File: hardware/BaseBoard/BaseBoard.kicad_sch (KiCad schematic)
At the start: 91 parts, among them J1 I2C, J1-ESP1 ESP-1-L, J1-ESP2 ESP-1-L, J1-ESP3 ESP-1-L, J1-ESP4 ESP-1-L, J1-ESP5 ESP-1-L, J1-ESP6 ESP-1-L, J1-ESP7 ESP-1-L, J1-ESP8 ESP-1-L, J2 3V3P0_7, J2-ESP1 ESP-1-R, J2-ESP2 ESP-1-R, J2-ESP3 ESP-1-R, J2-ESP4 ESP-1-R, J2-ESP5 ESP-1-R, J2-ESP6 ESP-1-R, J2-ESP7 ESP-1-R, J2-ESP8 ESP-1-R, J3-BUS1 BUS1-IN1, J3-BUS2 BUS1-IN1, J3-BUS3 BUS1-IN1, J3-BUS4 BUS1-IN1, J3-BUS5 BUS1-IN1, J3-BUS6 BUS1-IN1, J3-BUS7 BUS1-IN1, J3-BUS8 BUS1-IN1, J4-BUS1 BUS1-IN2, J4-BUS2 BUS1-IN2, J4-BUS3 BUS1-IN2, J4-BUS4 BUS1-IN2, J4-BUS5 BUS1-IN2, J4-BUS6 BUS1-IN2, J4-BUS7 BUS1-IN2, J4-BUS8 BUS1-IN2, J5-BUS1 BUS1-OUT, J5-BUS2 BUS1-OUT, J5-BUS3 BUS1-OUT, J5-BUS4 BUS1-OUT, J5-BUS5 BUS1-OUT, J5-BUS6 BUS1-OUT, J5-BUS7 BUS1-OUT, J5-BUS8 BUS1-OUT, Q1-ESP1 2N3904, Q1-ESP2 2N3904, Q1-ESP3 2N3904, Q1-ESP4 2N3904, Q1-ESP5 2N3904, Q1-ESP6 2N3904, Q1-ESP7 2N3904, Q1-ESP8 2N3904, Q2-ESP1 AO3401A, Q2-ESP2 AO3401A, Q2-ESP3 AO3401A, Q2-ESP4 AO3401A, Q2-ESP5 AO3401A, Q2-ESP6 AO3401A, Q2-ESP7 AO3401A, Q2-ESP8 AO3401A, U1 AMS1117-3.3

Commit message: Small optimizations.
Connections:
- net +5V: now also SW-ESP1.6, SW-ESP2.6, SW-ESP3.6, SW-ESP4.6, SW-ESP5.6, SW-ESP6.6, SW-ESP7.6, SW-ESP8.6
- net SWPIN-ESP5: now also J2.8 (Pin_8); no longer J2.5 (Pin_5)
- net SWPIN-ESP6: now also J2.7 (Pin_7); no longer J2.6 (Pin_6)
- net SWPIN-ESP7: now also J2.6 (Pin_6); no longer J2.7 (Pin_7)
- net SWPIN-ESP8: now also J2.5 (Pin_5); no longer J2.8 (Pin_8)
- no-connect marks 97 -> 89

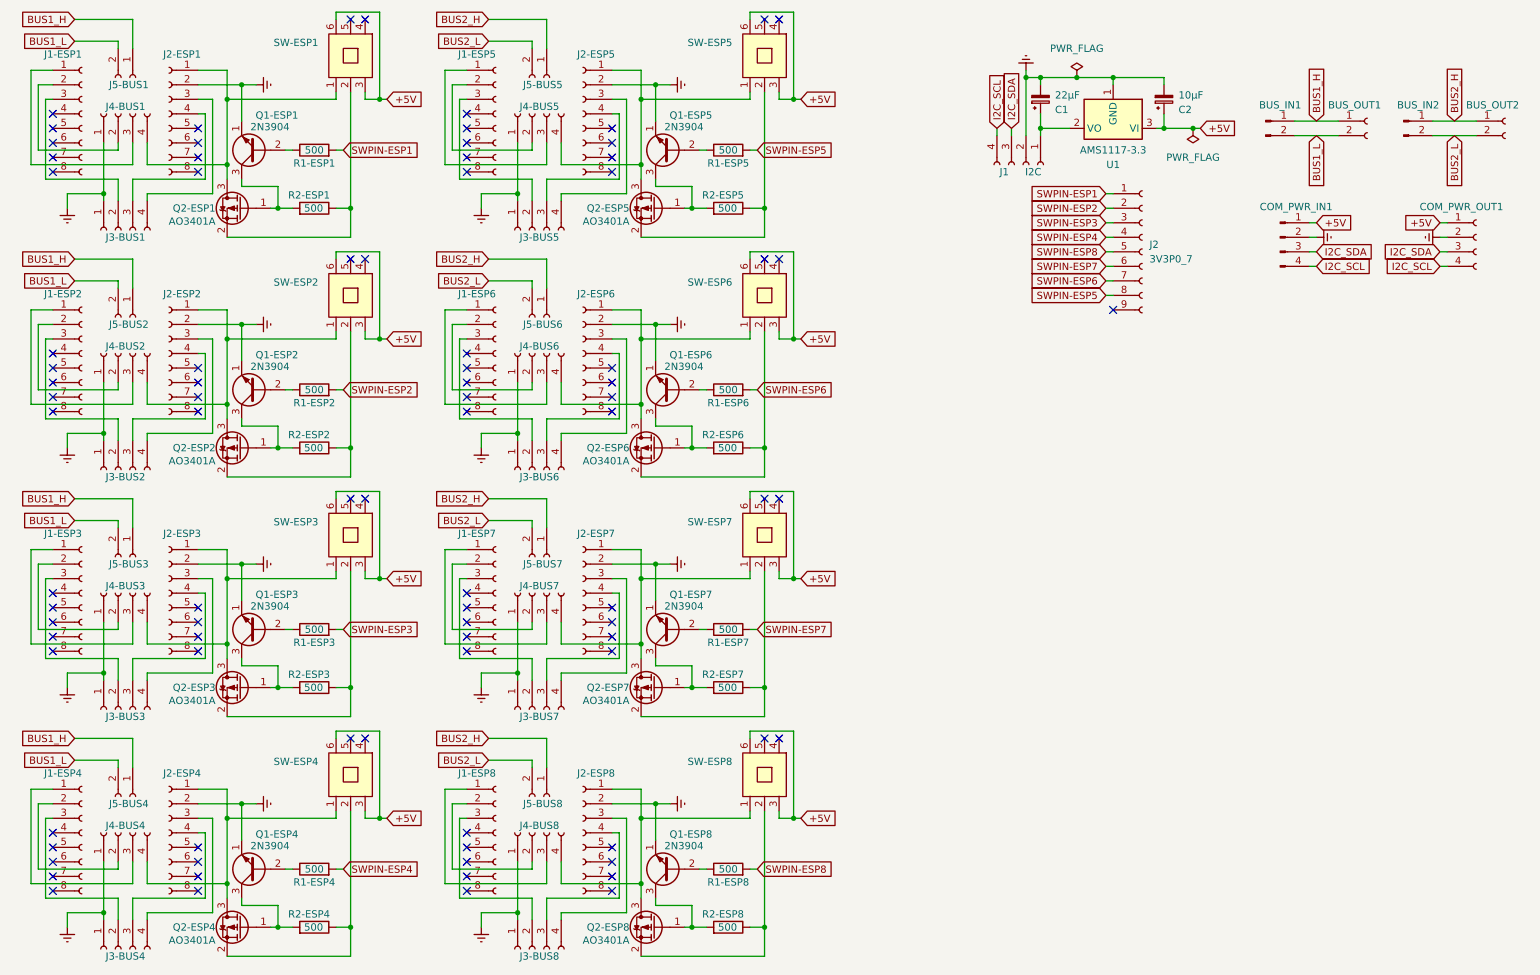
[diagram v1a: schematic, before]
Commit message: Added some more labels.
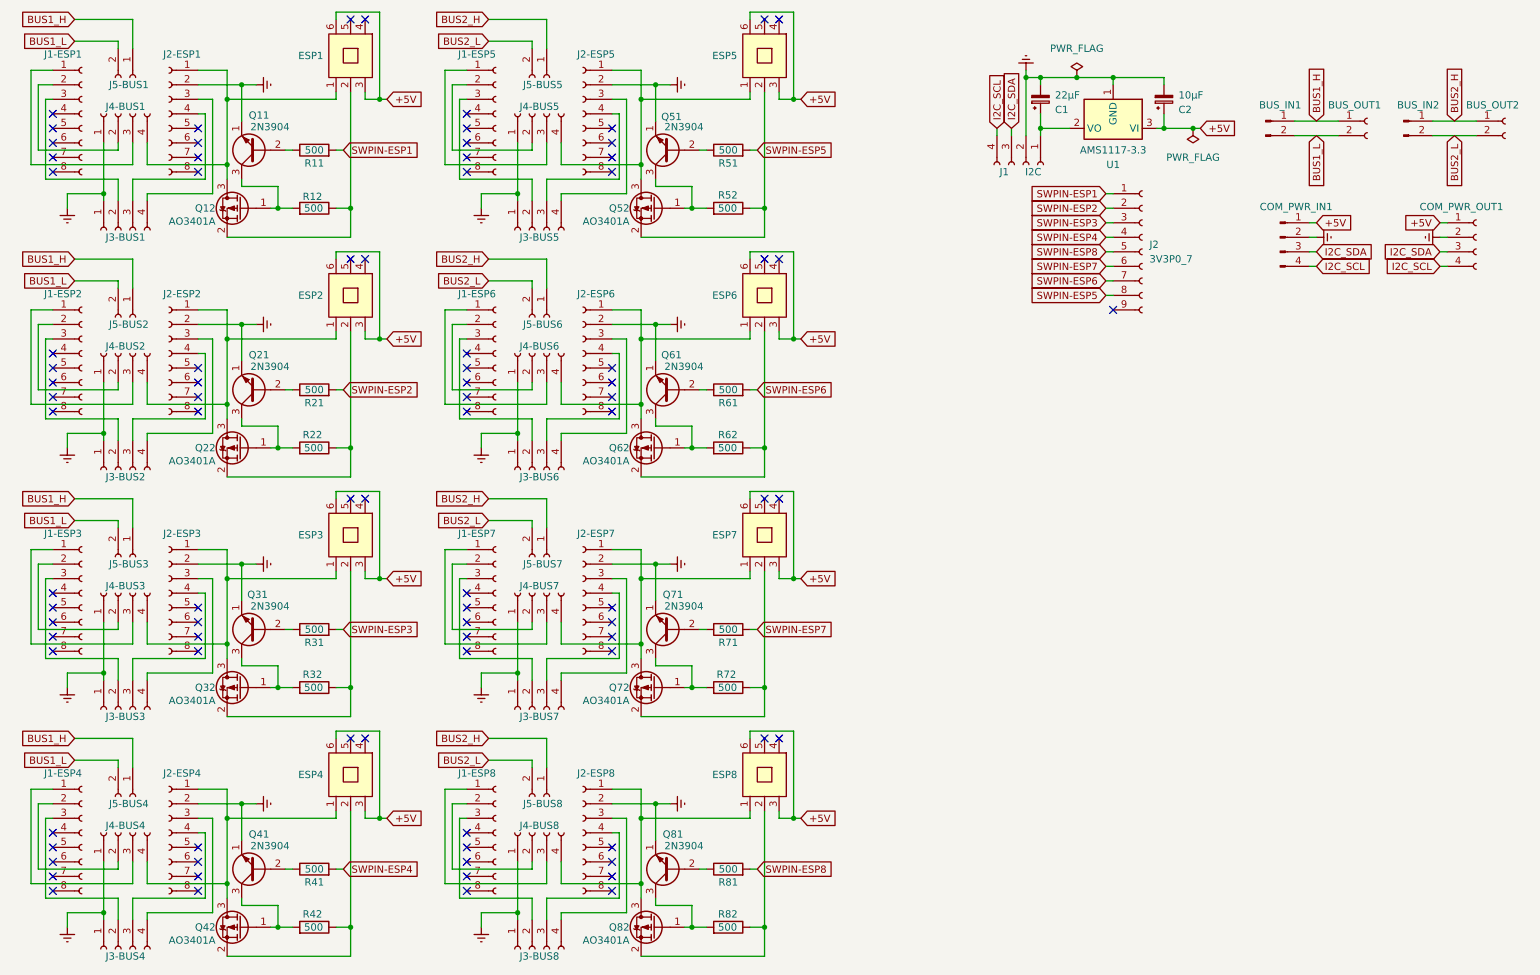
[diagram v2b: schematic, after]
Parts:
- renumbered SW-ESP1 to ESP1, SW-ESP2 to ESP2, SW-ESP3 to ESP3, SW-ESP4 to ESP4, SW-ESP5 to ESP5, SW-ESP6 to ESP6, SW-ESP7 to ESP7, SW-ESP8 to ESP8, Q1-ESP1 to Q11, Q2-ESP1 to Q12, Q1-ESP2 to Q21, Q2-ESP2 to Q22, Q1-ESP3 to Q31, Q2-ESP3 to Q32, Q1-ESP4 to Q41, Q2-ESP4 to Q42, Q1-ESP5 to Q51, Q2-ESP5 to Q52, Q1-ESP6 to Q61, Q2-ESP6 to Q62, Q1-ESP7 to Q71, Q2-ESP7 to Q72, Q1-ESP8 to Q81, Q2-ESP8 to Q82, R1-ESP1 to R11, R2-ESP1 to R12, R1-ESP2 to R21, R2-ESP2 to R22, R1-ESP3 to R31, R2-ESP3 to R32, R1-ESP4 to R41, R2-ESP4 to R42, R1-ESP5 to R51, R2-ESP5 to R52, R1-ESP6 to R61, R2-ESP6 to R62, R1-ESP7 to R71, R2-ESP7 to R72, R1-ESP8 to R81, R2-ESP8 to R82

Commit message: Replaced two one row headers with one two row header.
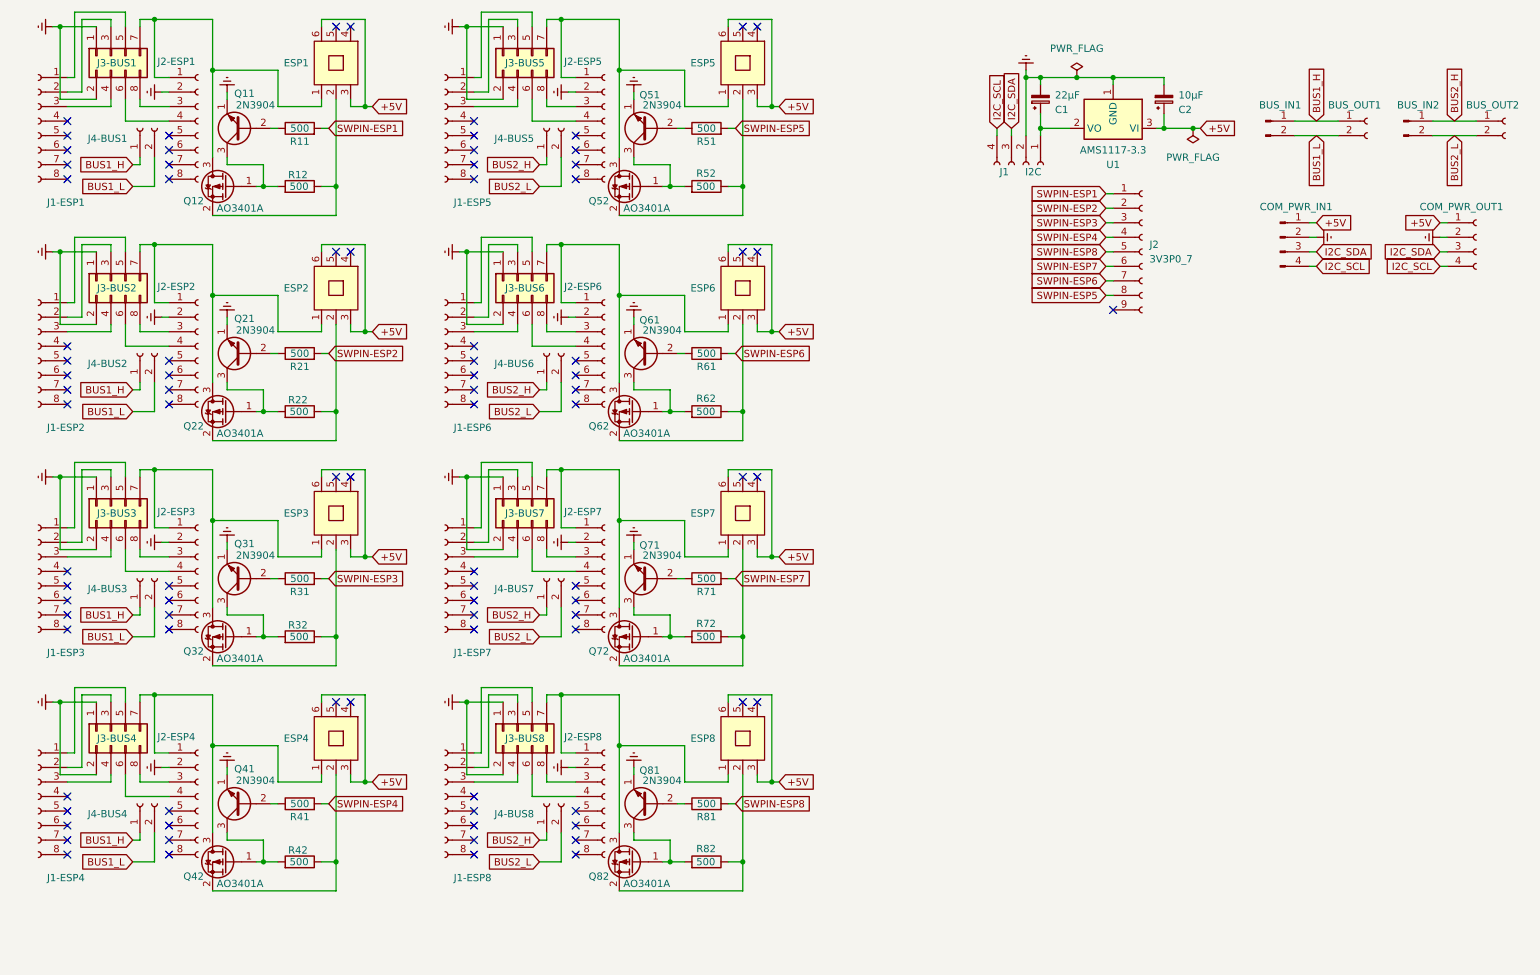
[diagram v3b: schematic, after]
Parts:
- removed J3-BUS1, J3-BUS2, J3-BUS3, J3-BUS4, J3-BUS6, J3-BUS7, J3-BUS8: BUS1-IN1, Connector_PinSocket_2.54mm:PinSocket_1x04_P2.54mm_Vertical, symbol Connector:Conn_01x04_Socket
- removed J4-BUS1, J4-BUS2, J4-BUS3, J4-BUS4, J4-BUS5, J4-BUS6, J4-BUS7, J4-BUS8: BUS1-IN2, Connector_PinSocket_2.54mm:PinSocket_1x04_P2.54mm_Vertical, symbol Connector:Conn_01x04_Socket
- removed J5-BUS2, J5-BUS3, J5-BUS4, J5-BUS6, J5-BUS7, J5-BUS8: BUS1-OUT, Connector_PinSocket_2.54mm:PinSocket_1x02_P2.54mm_Vertical, symbol Connector:Conn_01x02_Socket
- added J3-BUS1, J3-BUS2, J3-BUS3, J3-BUS4: BUS1-IN, Connector_PinSocket_2.54mm:PinSocket_2x04_P2.54mm_Vertical, symbol Connector_Generic:Conn_02x04_Odd_Even
- added J3-BUS6, J3-BUS7, J3-BUS8: BUS5-IN, Connector_PinSocket_2.54mm:PinSocket_2x04_P2.54mm_Vertical, symbol Connector_Generic:Conn_02x04_Odd_Even
- added J4-BUS2, J4-BUS3, J4-BUS4, J4-BUS6, J4-BUS7, J4-BUS8: BUS1-OUT, Connector_PinSocket_2.54mm:PinSocket_1x02_P2.54mm_Vertical, symbol Connector:Conn_01x02_Socket
- J3-BUS5: value BUS1-IN1 -> BUS5-IN; footprint Connector_PinSocket_2.54mm:PinSocket_1x04_P2.54mm_Vertical -> Connector_PinSocket_2.54mm:PinSocket_2x04_P2.54mm_Vertical; symbol Connector:Conn_01x04_Socket -> Connector_Generic:Conn_02x04_Odd_Even
- renumbered J5-BUS1 to J4-BUS1, J5-BUS5 to J4-BUS5
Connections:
- net BUS1_H: now also J4-BUS2.1 (Pin_1), J4-BUS3.1 (Pin_1), J4-BUS4.1 (Pin_1)
- net BUS1_L: now also J4-BUS2.2 (Pin_2), J4-BUS3.2 (Pin_2), J4-BUS4.2 (Pin_2)
- net BUS2_H: now also J4-BUS6.1 (Pin_1), J4-BUS7.1 (Pin_1), J4-BUS8.1 (Pin_1)
- net BUS2_L: now also J4-BUS6.2 (Pin_2), J4-BUS7.2 (Pin_2), J4-BUS8.2 (Pin_2)
- net GNDREF: now also J3-BUS5.2 (Pin_2), J3-BUS1.1 (Pin_1), J3-BUS1.2 (Pin_2), J3-BUS2.1 (Pin_1), J3-BUS2.2 (Pin_2), J3-BUS3.1 (Pin_1), J3-BUS3.2 (Pin_2), J3-BUS4.1 (Pin_1), J3-BUS4.2 (Pin_2), J3-BUS6.1 (Pin_1), J3-BUS6.2 (Pin_2), J3-BUS7.1 (Pin_1), J3-BUS7.2 (Pin_2), J3-BUS8.1 (Pin_1), J3-BUS8.2 (Pin_2)
- net at J1-ESP7.1 (Pin_1): now also J3-BUS7.5 (Pin_5)
- net at J1-ESP7.2 (Pin_2): now also J3-BUS7.3 (Pin_3)
- net at J1-ESP7.3 (Pin_3): now also J3-BUS7.4 (Pin_4)
- net at J1-ESP3.1 (Pin_1): now also J3-BUS3.5 (Pin_5)
- net at J1-ESP3.2 (Pin_2): now also J3-BUS3.3 (Pin_3)
- net at J1-ESP3.3 (Pin_3): now also J3-BUS3.4 (Pin_4)
- net at ESP6.1, J2-ESP6.1 (Pin_1), Q62.3 (D): now also J3-BUS6.7 (Pin_7)
- net at J1-ESP1.3 (Pin_3): now also J3-BUS1.4 (Pin_4)
- net at J2-ESP1.4 (Pin_4): now also J3-BUS1.6 (Pin_6)
- net at J2-ESP1.3 (Pin_3): now also J3-BUS1.8 (Pin_8)
- net at J1-ESP4.1 (Pin_1): now also J3-BUS4.5 (Pin_5)
- net at J1-ESP4.2 (Pin_2): now also J3-BUS4.3 (Pin_3)
- net at J1-ESP4.3 (Pin_3): now also J3-BUS4.4 (Pin_4)
- net at J2-ESP4.4 (Pin_4): now also J3-BUS4.6 (Pin_6)
- net at J2-ESP4.3 (Pin_3): now also J3-BUS4.8 (Pin_8)
- net at J1-ESP6.2 (Pin_2): now also J3-BUS6.3 (Pin_3)
- net at J1-ESP6.1 (Pin_1): now also J3-BUS6.5 (Pin_5)
- net at ESP4.1, J2-ESP4.1 (Pin_1), Q42.3 (D): now also J3-BUS4.7 (Pin_7)
- net at ESP8.1, J2-ESP8.1 (Pin_1), Q82.3 (D): now also J3-BUS8.7 (Pin_7)
- net at J2-ESP8.3 (Pin_3): now also J3-BUS8.8 (Pin_8)
- net at J2-ESP8.4 (Pin_4): now also J3-BUS8.6 (Pin_6)
- net at ESP5.1, J2-ESP5.1 (Pin_1), Q52.3 (D): now also J3-BUS5.7 (Pin_7)
- net at ESP2.1, J2-ESP2.1 (Pin_1), Q22.3 (D): now also J3-BUS2.7 (Pin_7)
- net at J2-ESP2.3 (Pin_3): now also J3-BUS2.8 (Pin_8)
- net at J2-ESP2.4 (Pin_4): now also J3-BUS2.6 (Pin_6)
- net at ESP7.1, J2-ESP7.1 (Pin_1), Q72.3 (D): now also J3-BUS7.7 (Pin_7)
- net at ESP1.1, J2-ESP1.1 (Pin_1), Q12.3 (D): now also J3-BUS1.7 (Pin_7)
- net at J2-ESP3.4 (Pin_4): now also J3-BUS3.6 (Pin_6)
- net at J2-ESP3.3 (Pin_3): now also J3-BUS3.8 (Pin_8)
- net at J1-ESP8.2 (Pin_2): now also J3-BUS8.3 (Pin_3)
- net at J1-ESP8.1 (Pin_1): now also J3-BUS8.5 (Pin_5)
- net at J1-ESP6.3 (Pin_3): now also J3-BUS6.4 (Pin_4)
- net at J1-ESP8.3 (Pin_3): now also J3-BUS8.4 (Pin_4)
- net at J2-ESP7.4 (Pin_4): now also J3-BUS7.6 (Pin_6)
- net at J2-ESP7.3 (Pin_3): now also J3-BUS7.8 (Pin_8)
- net at J1-ESP2.3 (Pin_3): now also J3-BUS2.4 (Pin_4)
- net at J1-ESP5.2 (Pin_2): now also J3-BUS5.3 (Pin_3)
- net at J1-ESP5.1 (Pin_1): now also J3-BUS5.5 (Pin_5)
- net at ESP3.1, J2-ESP3.1 (Pin_1), Q32.3 (D): now also J3-BUS3.7 (Pin_7)
- net at J1-ESP1.2 (Pin_2): now also J3-BUS1.3 (Pin_3)
- net at J1-ESP1.1 (Pin_1): now also J3-BUS1.5 (Pin_5)
- net at J1-ESP5.3 (Pin_3): now also J3-BUS5.4 (Pin_4); no longer J3-BUS5.2 (Pin_2)
- net at J2-ESP5.4 (Pin_4): now also J3-BUS5.6 (Pin_6); no longer J3-BUS5.3 (Pin_3)
- net at J2-ESP5.3 (Pin_3): now also J3-BUS5.8 (Pin_8); no longer J3-BUS5.4 (Pin_4)
- net at J2-ESP6.3 (Pin_3): now also J3-BUS6.8 (Pin_8)
- net at J2-ESP6.4 (Pin_4): now also J3-BUS6.6 (Pin_6)
- net at J1-ESP2.2 (Pin_2): now also J3-BUS2.3 (Pin_3)
- net at J1-ESP2.1 (Pin_1): now also J3-BUS2.5 (Pin_5)
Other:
- moved on the sheet: ESP1, ESP5, J1-ESP1, J1-ESP5, J2-ESP1, J2-ESP5, J4-BUS1, J4-BUS5, Q11, Q12, Q51, Q52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

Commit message: Cosmetics.
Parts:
- J3-BUS1, J3-BUS2, J3-BUS3, J3-BUS4: value BUS1-IN -> BUS-IN
- J3-BUS5, J3-BUS6, J3-BUS7, J3-BUS8: value BUS5-IN -> BUS-IN
- J4-BUS1, J4-BUS2, J4-BUS3, J4-BUS4, J4-BUS5, J4-BUS6, J4-BUS7, J4-BUS8: value BUS1-OUT -> BUS-OUT
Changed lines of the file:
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@@
 			)
 		)
-		(property "Value" "BUS5-IN"
+		(property "Value" "BUS-IN"
 			(at 101.6 101.6 90)
 			(effects
@@
 			)
 		)
-		(property "Value" "BUS1-IN"
+		(property "Value" "BUS-IN"
 			(at 22.86 62.23 0)
 			(effects
@@
 			)
 		)
-		(property "Value" "BUS1-IN"
+		(property "Value" "BUS-IN"
 			(at 22.86 22.86 0)
 			(effects
@@
 			)
 		)
-		(property "Value" "BUS5-IN"
+		(property "Value" "BUS-IN"
 			(at 101.6 140.97 90)
 			(effects
@@
 			)
 		)
-		(property "Value" "BUS1-OUT"
+		(property "Value" "BUS-OUT"
 			(at 32.512 111.506 90)
 			(effects
@@
 			)
 		)
-		(property "Value" "BUS1-OUT"
+		(property "Value" "BUS-OUT"
 			(at 103.632 150.876 90)
 			(effects
@@
 			)
 		)
-		(property "Value" "BUS1-OUT"
+		(property "Value" "BUS-OUT"
 			(at 32.512 32.766 90)
 			(effects
@@
 			)
 		)
-		(property "Value" "BUS1-OUT"
+		(property "Value" "BUS-OUT"
 			(at 32.512 72.136 90)
 			(effects
@@
 			)
 		)
-		(property "Value" "BUS1-IN"
+		(property "Value" "BUS-IN"
 			(at 22.86 101.6 0)
 			(effects
@@
 			)
 		)
-		(property "Value" "BUS5-IN"
+		(property "Value" "BUS-IN"
 			(at 101.6 62.23 90)
 			(effects
@@
 			)
 		)
-		(property "Value" "BUS1-OUT"
+		(property "Value" "BUS-OUT"
 			(at 32.512 150.876 90)
 			(effects
@@
 			)
 		)
-		(property "Value" "BUS1-OUT"
+		(property "Value" "BUS-OUT"
 			(at 103.632 72.136 90)
 			(effects
@@
 			)
 		)
-		(property "Value" "BUS1-OUT"
+		(property "Value" "BUS-OUT"
 			(at 103.632 32.766 90)
 			(effects
@@
 			)
 		)
-		(property "Value" "BUS5-IN"
+		(property "Value" "BUS-IN"
 			(at 101.6 22.86 90)
 			(effects
@@
 			)
 		)
-		(property "Value" "BUS1-OUT"
+		(property "Value" "BUS-OUT"
 			(at 103.632 111.506 90)
 			(effects
@@
 			)
 		)
-		(property "Value" "BUS1-IN"
+		(property "Value" "BUS-IN"
 			(at 22.86 140.97 0)
 			(effects

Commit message: BaseBoard v1.1 update.
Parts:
- removed J1: I2C, Connector_PinSocket_2.54mm:PinSocket_1x04_P2.54mm_Vertical, symbol Connector:Conn_01x04_Socket
- removed J2: 3V3P0_7, Connector_PinSocket_2.54mm:PinSocket_1x09_P2.54mm_Vertical, symbol Connector:Conn_01x09_Socket
- added IC1: PCF8574RGTR, LIB_PCF8574RGTR:QFN50P300X300X100-17N-D, symbol PCF8574RGTR:PCF8574RGTR
- added R1, R2, R3, R4, R5, R6: 10k, Resistor_SMD:R_0201_0603Metric, symbol Device:R
- added SW1: SW_DIP_SPSTx03, Button_Switch_SMD:SW_DIP_SPSTx03_Slide_6.7x9.18mm_W8.61mm_P2.54mm_LowProfile, symbol Switch:SW_DIP_x03
- BUS_IN1, BUS_IN2, BUS_OUT1, BUS_OUT2, COM_PWR_IN1, COM_PWR_OUT1, ESP1, ESP2, ESP3, ESP4, ESP5, ESP6, ESP7, ESP8, J1-ESP1, J1-ESP2, J1-ESP3, J1-ESP4, J1-ESP5, J1-ESP6, J1-ESP7, J1-ESP8, J2-ESP1, J2-ESP2, J2-ESP3, J2-ESP4, J2-ESP5, J2-ESP6, J2-ESP7, J2-ESP8, J3-BUS1, J3-BUS2, J3-BUS3, J3-BUS4, J3-BUS5, J3-BUS6, J3-BUS7, J3-BUS8, J4-BUS1, J4-BUS2, J4-BUS3, J4-BUS4, J4-BUS5, J4-BUS6, J4-BUS7, J4-BUS8, Q11, Q21, Q31, Q41, Q51, Q61, Q71, Q81: now left out of the parts list
- C1, C2: footprint Capacitor_THT:CP_Radial_D6.3mm_P2.50mm -> Capacitor_SMD:CP_Elec_4x5.3
- R11, R12, R21, R22, R31, R32, R41, R42, R51, R52, R61, R62, R71, R72, R81, R82: footprint Resistor_THT:R_Axial_DIN0207_L6.3mm_D2.5mm_P7.62mm_Horizontal -> Resistor_SMD:R_0603_1608Metric
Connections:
- net GNDREF: now also IC1.17 (GND_2), IC1.9 (GND_1), R4.2, R5.2, R6.2; no longer J3-BUS1.2 (Pin_2), J3-BUS2.2 (Pin_2), J3-BUS3.2 (Pin_2), J3-BUS4.2 (Pin_2), J3-BUS5.2 (Pin_2), J3-BUS6.2 (Pin_2), J3-BUS7.2 (Pin_2), J3-BUS8.2 (Pin_2)
- net I2C_SCL: now also IC1.15 (SCL), R1.1
- net I2C_SDA: now also IC1.16 (SDA), R2.1
- net SWPIN-ESP1: now also IC1.13 (P7)
- net SWPIN-ESP2: now also IC1.12 (P6)
- net SWPIN-ESP3: now also IC1.11 (P5)
- net SWPIN-ESP4: now also IC1.10 (P4)
- net SWPIN-ESP5: now also IC1.8 (P3)
- net SWPIN-ESP6: now also IC1.7 (P2)
- net SWPIN-ESP7: now also IC1.6 (P1)
- net SWPIN-ESP8: now also IC1.5 (P0)
- net +3V3: now reaches C1.1, U1.2 (VO)
- net +3V3: now also IC1.1 (VCC), R1.2, R2.2, R3.2, SW1.4, SW1.5, SW1.6
- net at J1-ESP2.6 (Pin_6): now also J3-BUS2.2 (Pin_2)
- net at J1-ESP4.6 (Pin_6): now also J3-BUS4.2 (Pin_2)
- net at J1-ESP6.6 (Pin_6): now also J3-BUS6.2 (Pin_2)
- net at J1-ESP7.6 (Pin_6): now also J3-BUS7.2 (Pin_2)
- net at J1-ESP3.6 (Pin_6): now also J3-BUS3.2 (Pin_2)
- net at J1-ESP5.6 (Pin_6): now also J3-BUS5.2 (Pin_2)
- net at J1-ESP8.6 (Pin_6): now also J3-BUS8.2 (Pin_2)
- net at J1-ESP1.6 (Pin_6): now also J3-BUS1.2 (Pin_2)
- new net ADDR0: IC1.2 (A0), R4.1, SW1.3
- new net ADDR1: IC1.3 (A1), R5.1, SW1.2
- new net ADDR2: IC1.4 (A2), R6.1, SW1.1
- new net INT: IC1.14 (~{INT}), R3.1
- no-connect marks 89 -> 80
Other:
- moved on the sheet: C1, C2, U1

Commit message: Enlarged smallest SMD resistors.
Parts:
- R1, R2, R3, R4, R5, R6: footprint Resistor_SMD:R_0201_0603Metric -> Resistor_SMD:R_0402_1005Metric
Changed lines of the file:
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@@
 			)
 		)
-		(property "Footprint" "Resistor_SMD:R_0201_0603Metric"
+		(property "Footprint" "Resistor_SMD:R_0402_1005Metric"
 			(at 184.15 28.448 90)
 			(effects
@@
 			)
 		)
-		(property "Footprint" "Resistor_SMD:R_0201_0603Metric"
+		(property "Footprint" "Resistor_SMD:R_0402_1005Metric"
 			(at 185.42 53.848 90)
 			(effects
@@
 			)
 		)
-		(property "Footprint" "Resistor_SMD:R_0201_0603Metric"
+		(property "Footprint" "Resistor_SMD:R_0402_1005Metric"
 			(at 185.42 58.928 90)
 			(effects
@@
 			)
 		)
-		(property "Footprint" "Resistor_SMD:R_0201_0603Metric"
+		(property "Footprint" "Resistor_SMD:R_0402_1005Metric"
 			(at 184.15 23.368 90)
 			(effects
@@
 			)
 		)
-		(property "Footprint" "Resistor_SMD:R_0201_0603Metric"
+		(property "Footprint" "Resistor_SMD:R_0402_1005Metric"
 			(at 184.15 33.528 90)
 			(effects
@@
 			)
 		)
-		(property "Footprint" "Resistor_SMD:R_0201_0603Metric"
+		(property "Footprint" "Resistor_SMD:R_0402_1005Metric"
 			(at 185.42 48.768 90)
 			(effects
